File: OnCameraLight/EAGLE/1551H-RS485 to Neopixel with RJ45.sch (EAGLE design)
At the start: 8 parts, among them IC1 75176AP, J1 RJHSE-5381

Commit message: Go through and fix notation on RS485 wiring everywhere to use the standard A/B notation.
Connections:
- net DATA2+ renamed DATA2B
- net DATA2- renamed DATA2A
- net RS485+ renamed RS485B
- net RS485- renamed RS485A
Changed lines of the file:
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@@
-</segment>
-</net>
-<net name="RS485+" class="0">
-<segment>
-<pinref part="R1" gate="G$1" pin="1"/>
-<wire x1="124.46" y1="124.46" x2="116.84" y2="124.46" width="0.1524" layer="91"/>
-<label x="116.84" y="124.46" size="1.778" layer="95"/>
-</segment>
-<segment>
-<pinref part="IC1" gate="G$1" pin="B"/>
-<wire x1="91.44" y1="134.62" x2="104.14" y2="134.62" width="0.1524" layer="91"/>
-<label x="96.52" y="134.62" size="1.778" layer="95"/>
-</segment>
-<segment>
-<pinref part="J1" gate="G$1" pin="1"/>
-<wire x1="88.9" y1="87.63" x2="106.68" y2="87.63" width="0.1524" layer="91"/>
-<wire x1="106.68" y1="87.63" x2="106.68" y2="88.9" width="0.1524" layer="91"/>
-<label x="91.44" y="88.9" size="1.778" layer="95" align="center-left"/>
-</segment>
-</net>
-<net name="RS485-" class="0">
-<segment>
-<pinref part="R1" gate="G$1" pin="2"/>
-<wire x1="134.62" y1="124.46" x2="142.24" y2="124.46" width="0.1524" layer="91"/>
-<label x="134.62" y="124.46" size="1.778" layer="95"/>
-</segment>
-<segment>
-<pinref part="IC1" gate="G$1" pin="A"/>
-<wire x1="91.44" y1="137.16" x2="104.14" y2="137.16" width="0.1524" layer="91"/>
-<label x="96.52" y="137.16" size="1.778" layer="95"/>
-</segment>
-<segment>
-<pinref part="J1" gate="G$1" pin="2"/>
-<wire x1="88.9" y1="85.09" x2="106.68" y2="85.09" width="0.1524" layer="91"/>
-<wire x1="106.68" y1="85.09" x2="106.68" y2="86.36" width="0.1524" layer="91"/>
-<label x="91.44" y="86.36" size="1.778" layer="95" align="center-left"/>
 </segment>
 </net>
@@
 </segment>
 </net>
-<net name="DATA2+" class="0">
+<net name="DATA2B" class="0">
 <segment>
 <pinref part="J1" gate="G$1" pin="3"/>
@@
 </segment>
 </net>
-<net name="DATA2-" class="0">
+<net name="DATA2A" class="0">
 <segment>
 <pinref part="J1" gate="G$1" pin="6"/>
@@
 </segment>
 </net>
+<net name="RS485B" class="0">
+<segment>
+<pinref part="J1" gate="G$1" pin="1"/>
+<wire x1="88.9" y1="87.63" x2="106.68" y2="87.63" width="0.1524" layer="91"/>
+<wire x1="106.68" y1="87.63" x2="106.68" y2="88.9" width="0.1524" layer="91"/>
+<label x="91.44" y="88.9" size="1.778" layer="95" align="center-left"/>
+</segment>
+<segment>
+<pinref part="IC1" gate="G$1" pin="B"/>
+<wire x1="91.44" y1="134.62" x2="104.14" y2="134.62" width="0.1524" layer="91"/>
+<label x="96.52" y="134.62" size="1.778" layer="95"/>
+</segment>
+<segment>
+<pinref part="R1" gate="G$1" pin="1"/>
+<wire x1="124.46" y1="124.46" x2="116.84" y2="124.46" width="0.1524" layer="91"/>
+<label x="116.84" y="124.46" size="1.778" layer="95"/>
+</segment>
+</net>
+<net name="RS485A" class="0">
+<segment>
+<pinref part="J1" gate="G$1" pin="2"/>
+<wire x1="88.9" y1="85.09" x2="106.68" y2="85.09" width="0.1524" layer="91"/>
+<wire x1="106.68" y1="85.09" x2="106.68" y2="86.36" width="0.1524" layer="91"/>
+<label x="91.44" y="86.36" size="1.778" layer="95" align="center-left"/>
+</segment>
+<segment>
+<pinref part="IC1" gate="G$1" pin="A"/>
+<wire x1="91.44" y1="137.16" x2="104.14" y2="137.16" width="0.1524" layer="91"/>
+<label x="96.52" y="137.16" size="1.778" layer="95"/>
+</segment>
+<segment>
+<pinref part="R1" gate="G$1" pin="2"/>
+<wire x1="134.62" y1="124.46" x2="142.24" y2="124.46" width="0.1524" layer="91"/>
+<label x="134.62" y="124.46" size="1.778" layer="95"/>
+</segment>
+</net>

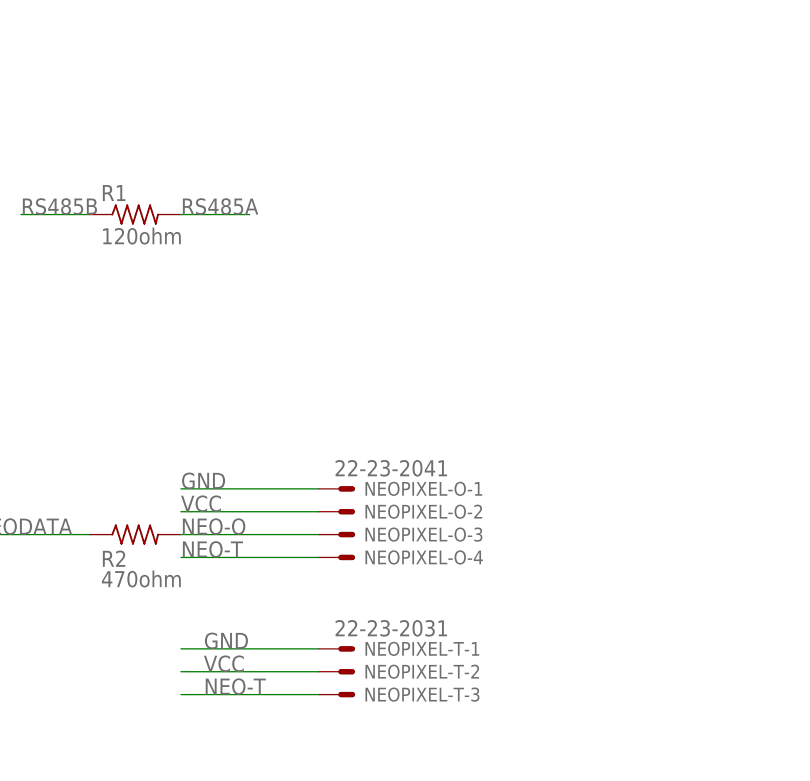
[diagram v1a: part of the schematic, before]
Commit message: Revisions to boards after working with initial prototypes.
- Update boards to use SMD components to help save on space.
- Redesign wireless receiver to use 3.3v logic to avoid using the Xbee breakout.
- Remove designs that aren't going to be used.
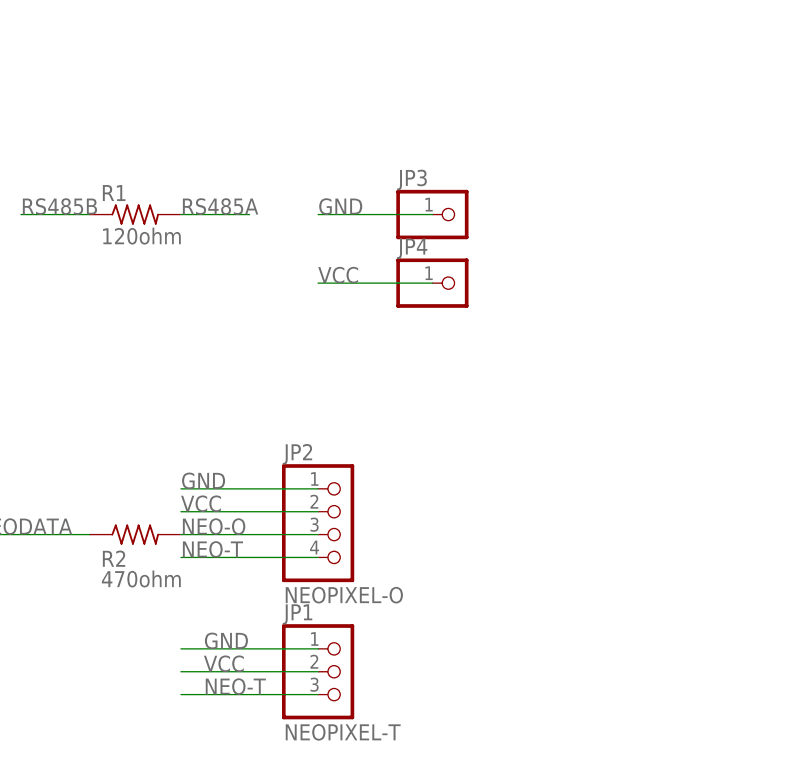
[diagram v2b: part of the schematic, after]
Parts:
- removed NEOPIXEL-O: 22-23-2041, con-molex:22-23-2041
- removed NEOPIXEL-T: 22-23-2031, con-molex:22-23-2031
- added JP1: NEOPIXEL-T, pinhead:PINHD-1X3
- added JP2: NEOPIXEL-O, pinhead:PINHD-1X4
- added JP3, JP4: (no value), pinhead:PINHD-1X1
- R1, R2: device rcl:R-US_0207/10 -> rcl:R-US_R0805
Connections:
- net GND: now also JP1.1, JP2.1, JP3.1; no longer NEOPIXEL-O-1.S, NEOPIXEL-T-1.S
- net NEO-O: now also JP2.3; no longer NEOPIXEL-O-3.S
- net NEO-T: now also JP1.3, JP2.4; no longer NEOPIXEL-O-4.S, NEOPIXEL-T-3.S
- net VCC: now also JP1.2, JP2.2, JP4.1; no longer NEOPIXEL-O-2.S, NEOPIXEL-T-2.S
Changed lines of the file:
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@@
 <parts>
 <part name="FRAME1" library="frames" library_urn="urn:adsk.eagle:library:229" deviceset="LETTER_L" device=""/>
-<part name="NEOPIXEL-T" library="con-molex" library_urn="urn:adsk.eagle:library:165" deviceset="22-23-2031" device="" package3d_urn="urn:adsk.eagle:package:8078634/1"/>
 <part name="IC1" library="751xx" library_urn="urn:adsk.eagle:library:89" deviceset="75176A" device="P" package3d_urn="urn:adsk.eagle:package:29519/2"/>
-<part name="R1" library="rcl" library_urn="urn:adsk.eagle:library:334" deviceset="R-US_" device="0207/10" package3d_urn="urn:adsk.eagle:package:23491/2" value="120ohm"/>
-<part name="R2" library="rcl" library_urn="urn:adsk.eagle:library:334" deviceset="R-US_" device="0207/10" package3d_urn="urn:adsk.eagle:package:23491/2" value="470ohm"/>
+<part name="R1" library="rcl" library_urn="urn:adsk.eagle:library:334" deviceset="R-US_" device="R0805" package3d_urn="urn:adsk.eagle:package:23553/2" value="120ohm"/>
+<part name="R2" library="rcl" library_urn="urn:adsk.eagle:library:334" deviceset="R-US_" device="R0805" package3d_urn="urn:adsk.eagle:package:23553/2" value="470ohm"/>
 <part name="C1" library="SparkFun-Capacitors" library_urn="urn:adsk.eagle:library:510" deviceset="1000UF" device="-RADIAL-5MM-25V-20%" package3d_urn="urn:adsk.eagle:package:37412/1" value="1000uf 16v"/>
 <part name="J1" library="RJHSE-5381" deviceset="RJHSE-5381" device=""/>
-<part name="NEOPIXEL-O" library="con-molex" library_urn="urn:adsk.eagle:library:165" deviceset="22-23-2041" device="" package3d_urn="urn:adsk.eagle:package:8078635/1"/>
 <part name="BOX1" library="hammond" deviceset="HAMMOND-BOX" device="-1551H"/>
+<part name="JP1" library="pinhead" library_urn="urn:adsk.eagle:library:325" deviceset="PINHD-1X3" device="" package3d_urn="urn:adsk.eagle:package:22458/2" value="NEOPIXEL-T"/>
+<part name="JP2" library="pinhead" library_urn="urn:adsk.eagle:library:325" deviceset="PINHD-1X4" device="" package3d_urn="urn:adsk.eagle:package:22407/2" value="NEOPIXEL-O"/>
+<part name="JP3" library="pinhead" library_urn="urn:adsk.eagle:library:325" deviceset="PINHD-1X1" device="" package3d_urn="urn:adsk.eagle:package:22485/2"/>
+<part name="JP4" library="pinhead" library_urn="urn:adsk.eagle:library:325" deviceset="PINHD-1X1" device="" package3d_urn="urn:adsk.eagle:package:22485/2"/>
 </parts>
 <sheets>
@@
 <attribute name="DRAWING_NAME" x="165.1" y="19.05" size="2.54" layer="94"/>
 </instance>
-<instance part="NEOPIXEL-T" gate="-1" x="152.4" y="76.2" smashed="yes">
-<attribute name="NAME" x="154.94" y="75.438" size="1.524" layer="95"/>
-<attribute name="VALUE" x="151.638" y="77.597" size="1.778" layer="96"/>
-</instance>
-<instance part="NEOPIXEL-T" gate="-2" x="152.4" y="73.66" smashed="yes">
-<attribute name="NAME" x="154.94" y="72.898" size="1.524" layer="95"/>
-</instance>
-<instance part="NEOPIXEL-T" gate="-3" x="152.4" y="71.12" smashed="yes">
-<attribute name="NAME" x="154.94" y="70.358" size="1.524" layer="95"/>
-</instance>
 <instance part="IC1" gate="G$1" x="78.74" y="137.16" smashed="yes">
 <attribute name="NAME" x="68.58" y="146.05" size="1.778" layer="95"/>
@@
 <attribute name="VALUE" x="76.1928" y="64.623" size="1.78051875" layer="96"/>
 </instance>
-<instance part="NEOPIXEL-O" gate="-1" x="152.4" y="93.98" smashed="yes">
-<attribute name="NAME" x="154.94" y="93.218" size="1.524" layer="95"/>
-<attribute name="VALUE" x="151.638" y="95.377" size="1.778" layer="96"/>
-</instance>
-<instance part="NEOPIXEL-O" gate="-2" x="152.4" y="91.44" smashed="yes">
-<attribute name="NAME" x="154.94" y="90.678" size="1.524" layer="95"/>
-</instance>
-<instance part="NEOPIXEL-O" gate="-3" x="152.4" y="88.9" smashed="yes">
-<attribute name="NAME" x="154.94" y="88.138" size="1.524" layer="95"/>
-</instance>
-<instance part="NEOPIXEL-O" gate="-4" x="152.4" y="86.36" smashed="yes">
-<attribute name="NAME" x="154.94" y="85.598" size="1.524" layer="95"/>
-</instance>
 <instance part="BOX1" gate="G$1" x="187.96" y="165.1" smashed="yes">
 <attribute name="NAME" x="193.04" y="165.1" size="1.778" layer="95"/>
 <attribute name="VALUE" x="182.88" y="154.94" size="1.778" layer="96"/>
+</instance>
+<instance part="JP1" gate="A" x="152.4" y="73.66" smashed="yes">
+<attribute name="NAME" x="146.05" y="79.375" size="1.778" layer="95"/>
+<attribute name="VALUE" x="146.05" y="66.04" size="1.778" layer="96"/>
+</instance>
+<instance part="JP2" gate="A" x="152.4" y="88.9" smashed="yes">
+<attribute name="NAME" x="146.05" y="97.155" size="1.778" layer="95"/>
+<attribute name="VALUE" x="146.05" y="81.28" size="1.778" layer="96"/>
+</instance>
+<instance part="JP3" gate="G$1" x="165.1" y="124.46" smashed="yes">
+<attribute name="NAME" x="158.75" y="127.635" size="1.778" layer="95"/>
+<attribute name="VALUE" x="158.75" y="119.38" size="1.778" layer="96"/>
+</instance>
+<instance part="JP4" gate="G$1" x="165.1" y="116.84" smashed="yes">
+<attribute name="NAME" x="158.75" y="120.015" size="1.778" layer="95"/>
+<attribute name="VALUE" x="158.75" y="111.76" size="1.778" layer="96"/>
 </instance>
 </instances>
@@
 <net name="GND" class="0">
 <segment>
-<pinref part="NEOPIXEL-T" gate="-1" pin="S"/>
 <wire x1="149.86" y1="76.2" x2="134.62" y2="76.2" width="0.1524" layer="91"/>
 <label x="137.16" y="76.2" size="1.778" layer="95"/>
+<pinref part="JP1" gate="A" pin="1"/>
 </segment>
 <segment>
@@
 </segment>
 <segment>
-<pinref part="NEOPIXEL-O" gate="-1" pin="S"/>
 <wire x1="149.86" y1="93.98" x2="134.62" y2="93.98" width="0.1524" layer="91"/>
 <label x="134.62" y="93.98" size="1.778" layer="95"/>
+<pinref part="JP2" gate="A" pin="1"/>
+</segment>
+<segment>
+<pinref part="JP3" gate="G$1" pin="1"/>
+<wire x1="162.56" y1="124.46" x2="149.86" y2="124.46" width="0.1524" layer="91"/>
+<label x="149.86" y="124.46" size="1.778" layer="95"/>
 </segment>
 </net>
 <net name="VCC" class="0">
 <segment>
-<pinref part="NEOPIXEL-T" gate="-2" pin="S"/>
 <wire x1="149.86" y1="73.66" x2="134.62" y2="73.66" width="0.1524" layer="91"/>
 <label x="137.16" y="73.66" size="1.778" layer="95"/>
+<pinref part="JP1" gate="A" pin="2"/>
 </segment>
 <segment>
@@
 </segment>
 <segment>
-<pinref part="NEOPIXEL-O" gate="-2" pin="S"/>
 <wire x1="149.86" y1="91.44" x2="134.62" y2="91.44" width="0.1524" layer="91"/>
 <label x="134.62" y="91.44" size="1.778" layer="95"/>
+<pinref part="JP2" gate="A" pin="2"/>
 </segment>
 <segment>
@@
 <label x="91.44" y="78.74" size="1.778" layer="95" align="center-left"/>
 </segment>
+<segment>
+<pinref part="JP4" gate="G$1" pin="1"/>
+<wire x1="162.56" y1="116.84" x2="149.86" y2="116.84" width="0.1524" layer="91"/>
+<label x="149.86" y="116.84" size="1.778" layer="95"/>
+</segment>
 </net>
 <net name="NEODATA" class="0">
@@
 <net name="NEO-T" class="0">
 <segment>
-<pinref part="NEOPIXEL-T" gate="-3" pin="S"/>
 <wire x1="149.86" y1="71.12" x2="134.62" y2="71.12" width="0.1524" layer="91"/>
 <label x="137.16" y="71.12" size="1.778" layer="95"/>
-</segment>
-<segment>
-<pinref part="NEOPIXEL-O" gate="-4" pin="S"/>
+<pinref part="JP1" gate="A" pin="3"/>
+</segment>
+<segment>
 <wire x1="149.86" y1="86.36" x2="134.62" y2="86.36" width="0.1524" layer="91"/>
 <label x="134.62" y="86.36" size="1.778" layer="95"/>
+<pinref part="JP2" gate="A" pin="4"/>
 </segment>
 </net>
 <net name="NEO-O" class="0">
 <segment>
-<pinref part="NEOPIXEL-O" gate="-3" pin="S"/>
 <wire x1="149.86" y1="88.9" x2="134.62" y2="88.9" width="0.1524" layer="91"/>
 <pinref part="R2" gate="G$1" pin="2"/>
 <label x="134.62" y="88.9" size="1.778" layer="95"/>
-</segment>
-</net>
+<pinref part="JP2" gate="A" pin="3"/>
+</segment>
+</net>

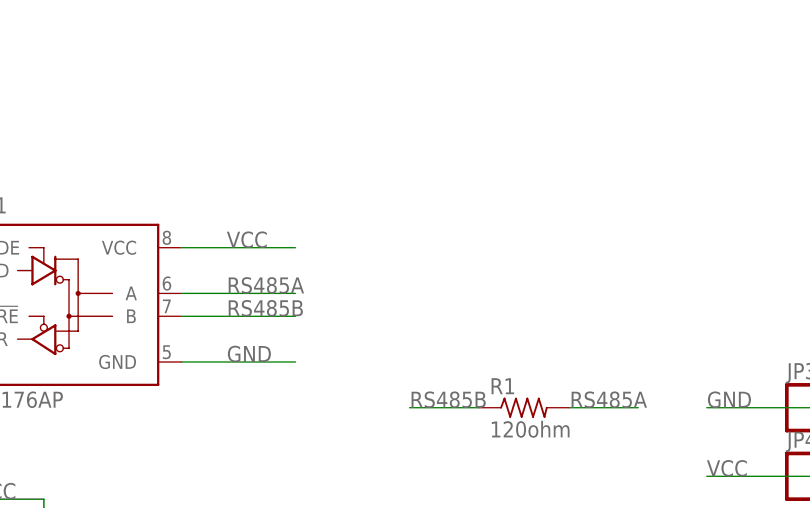
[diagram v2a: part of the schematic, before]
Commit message: Add decoupling caps
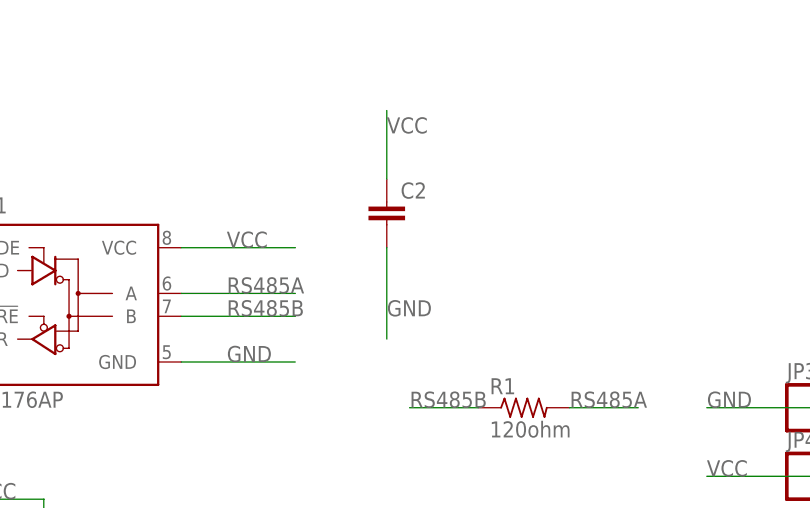
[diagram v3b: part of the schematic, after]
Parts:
- added C2: (no value), Nordic_nRF:CAPACITOR_0805_N
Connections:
- net GND: now also C2.2
- net VCC: now also C2.1
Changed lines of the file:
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@@
 <layer number="115" name="ReferenceISLANDS" color="7" fill="1" visible="yes" active="yes"/>
 <layer number="116" name="Patch_BOT" color="9" fill="4" visible="yes" active="yes"/>
+<layer number="117" name="BACKMAAT1" color="7" fill="1" visible="yes" active="yes"/>
 <layer number="118" name="Rect_Pads" color="7" fill="1" visible="yes" active="yes"/>
+<layer number="119" name="KAP_TEKEN" color="7" fill="1" visible="yes" active="yes"/>
+<layer number="120" name="KAP_MAAT1" color="7" fill="1" visible="yes" active="yes"/>
 <layer number="121" name="_tsilk" color="7" fill="1" visible="yes" active="yes"/>
 <layer number="122" name="_bsilk" color="7" fill="1" visible="yes" active="yes"/>
@@
 <layer number="128" name="_bValues" color="7" fill="1" visible="yes" active="yes"/>
 <layer number="129" name="Mask" color="7" fill="1" visible="yes" active="yes"/>
+<layer number="130" name="SMDSTROOK" color="7" fill="1" visible="yes" active="yes"/>
 <layer number="131" name="tAdjust" color="7" fill="1" visible="yes" active="yes"/>
 <layer number="132" name="bAdjust" color="7" fill="1" visible="yes" active="yes"/>
+<layer number="133" name="bottom_silk" color="7" fill="1" visible="yes" active="yes"/>
 <layer number="144" name="Drill_legend" color="7" fill="1" visible="yes" active="yes"/>
 <layer number="150" name="Notes" color="7" fill="1" visible="yes" active="yes"/>
@@
 <part name="JP3" library="pinhead" library_urn="urn:adsk.eagle:library:325" deviceset="PINHD-1X1" device="" package3d_urn="urn:adsk.eagle:package:22485/2"/>
 <part name="JP4" library="pinhead" library_urn="urn:adsk.eagle:library:325" deviceset="PINHD-1X1" device="" package3d_urn="urn:adsk.eagle:package:22485/2"/>
+<part name="C2" library="Nordic_nRF" library_urn="urn:adsk.eagle:library:169009" deviceset="CAPACITOR" device="_0805_N" package3d_urn="urn:adsk.eagle:package:2593736/1"/>
 </parts>
 <sheets>
@@
 <attribute name="VALUE" x="158.75" y="111.76" size="1.778" layer="96"/>
 </instance>
+<instance part="C2" gate="C$1" x="114.3" y="147.32" smashed="yes">
+<attribute name="NAME" x="115.824" y="147.701" size="1.778" layer="95"/>
+<attribute name="VALUE" x="115.824" y="142.621" size="1.778" layer="96"/>
+</instance>
 </instances>
 <busses>
@@
 <label x="149.86" y="124.46" size="1.778" layer="95"/>
 </segment>
+<segment>
+<pinref part="C2" gate="C$1" pin="2"/>
+<wire x1="114.3" y1="142.24" x2="114.3" y2="132.08" width="0.1524" layer="91"/>
+<label x="114.3" y="134.62" size="1.778" layer="95"/>
+</segment>
 </net>
 <net name="VCC" class="0">
@@
 <label x="149.86" y="116.84" size="1.778" layer="95"/>
 </segment>
+<segment>
+<pinref part="C2" gate="C$1" pin="1"/>
+<wire x1="114.3" y1="149.86" x2="114.3" y2="157.48" width="0.1524" layer="91"/>
+<label x="114.3" y="154.94" size="1.778" layer="95"/>
+</segment>
 </net>
